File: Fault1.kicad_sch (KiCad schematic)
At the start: 45 parts

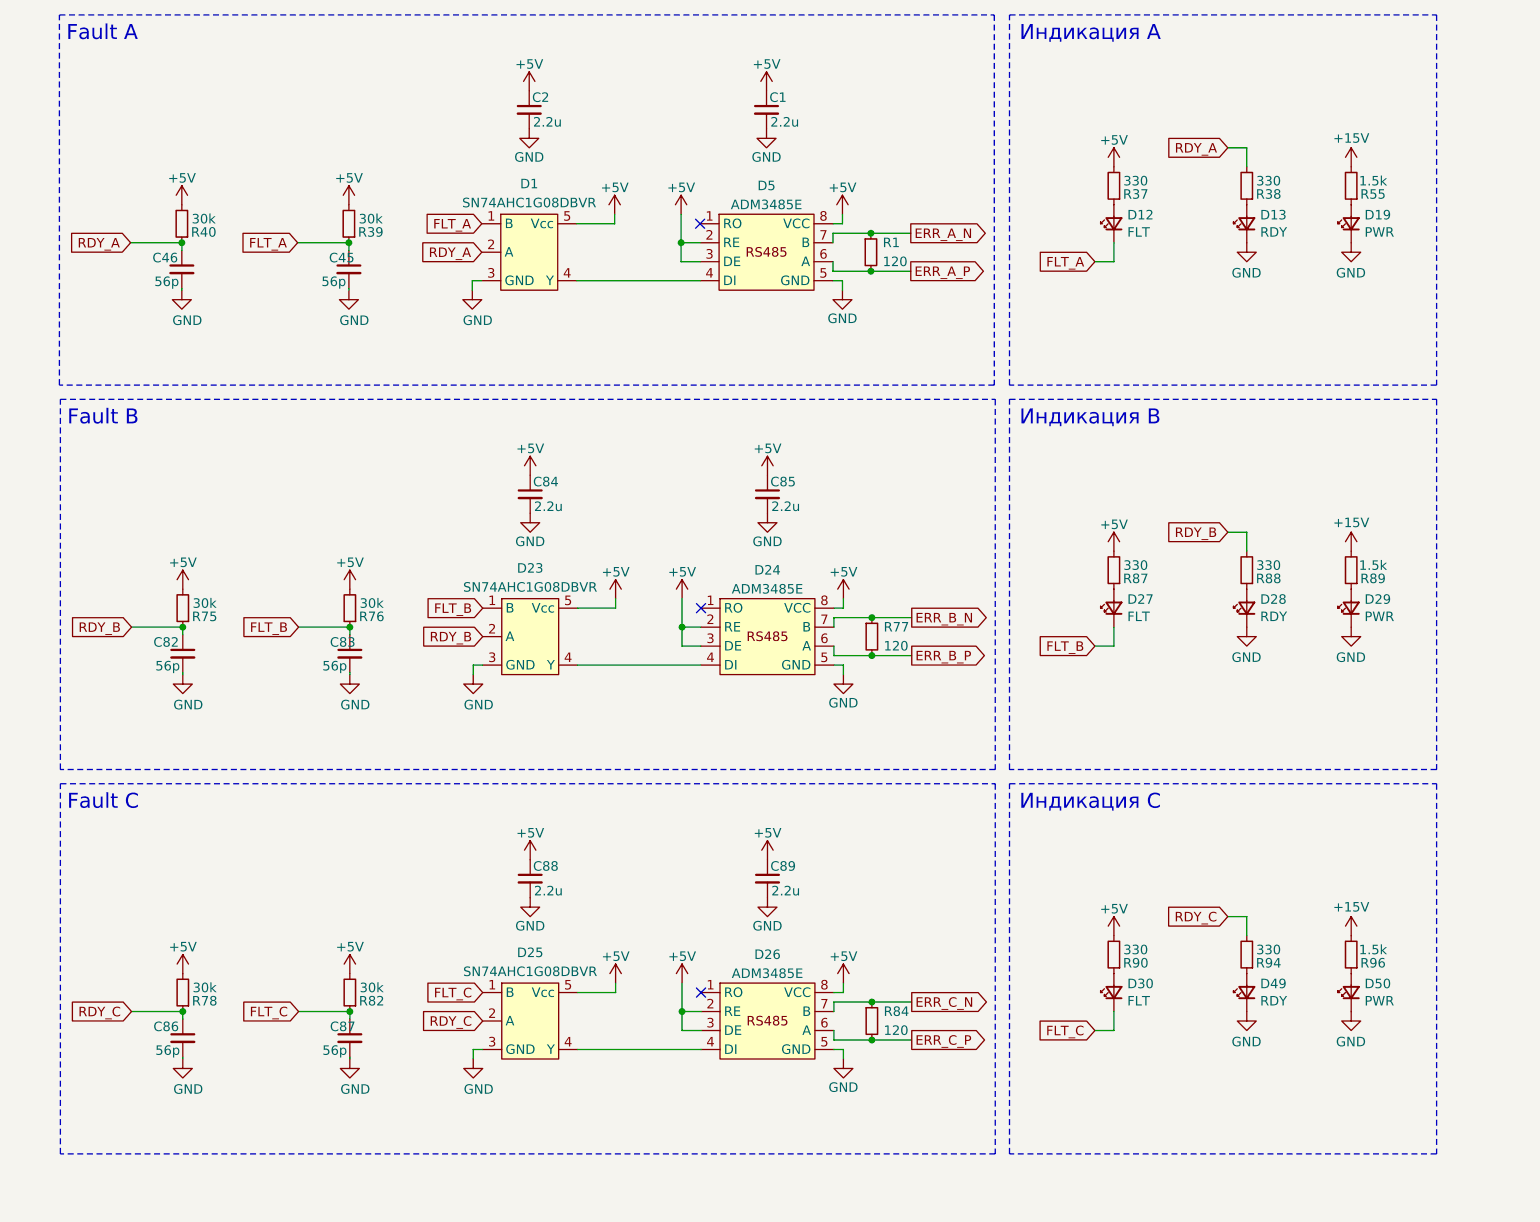
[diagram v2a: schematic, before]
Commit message: Исправления: исправил номиналы подтяжек и сопротивления светодиодов
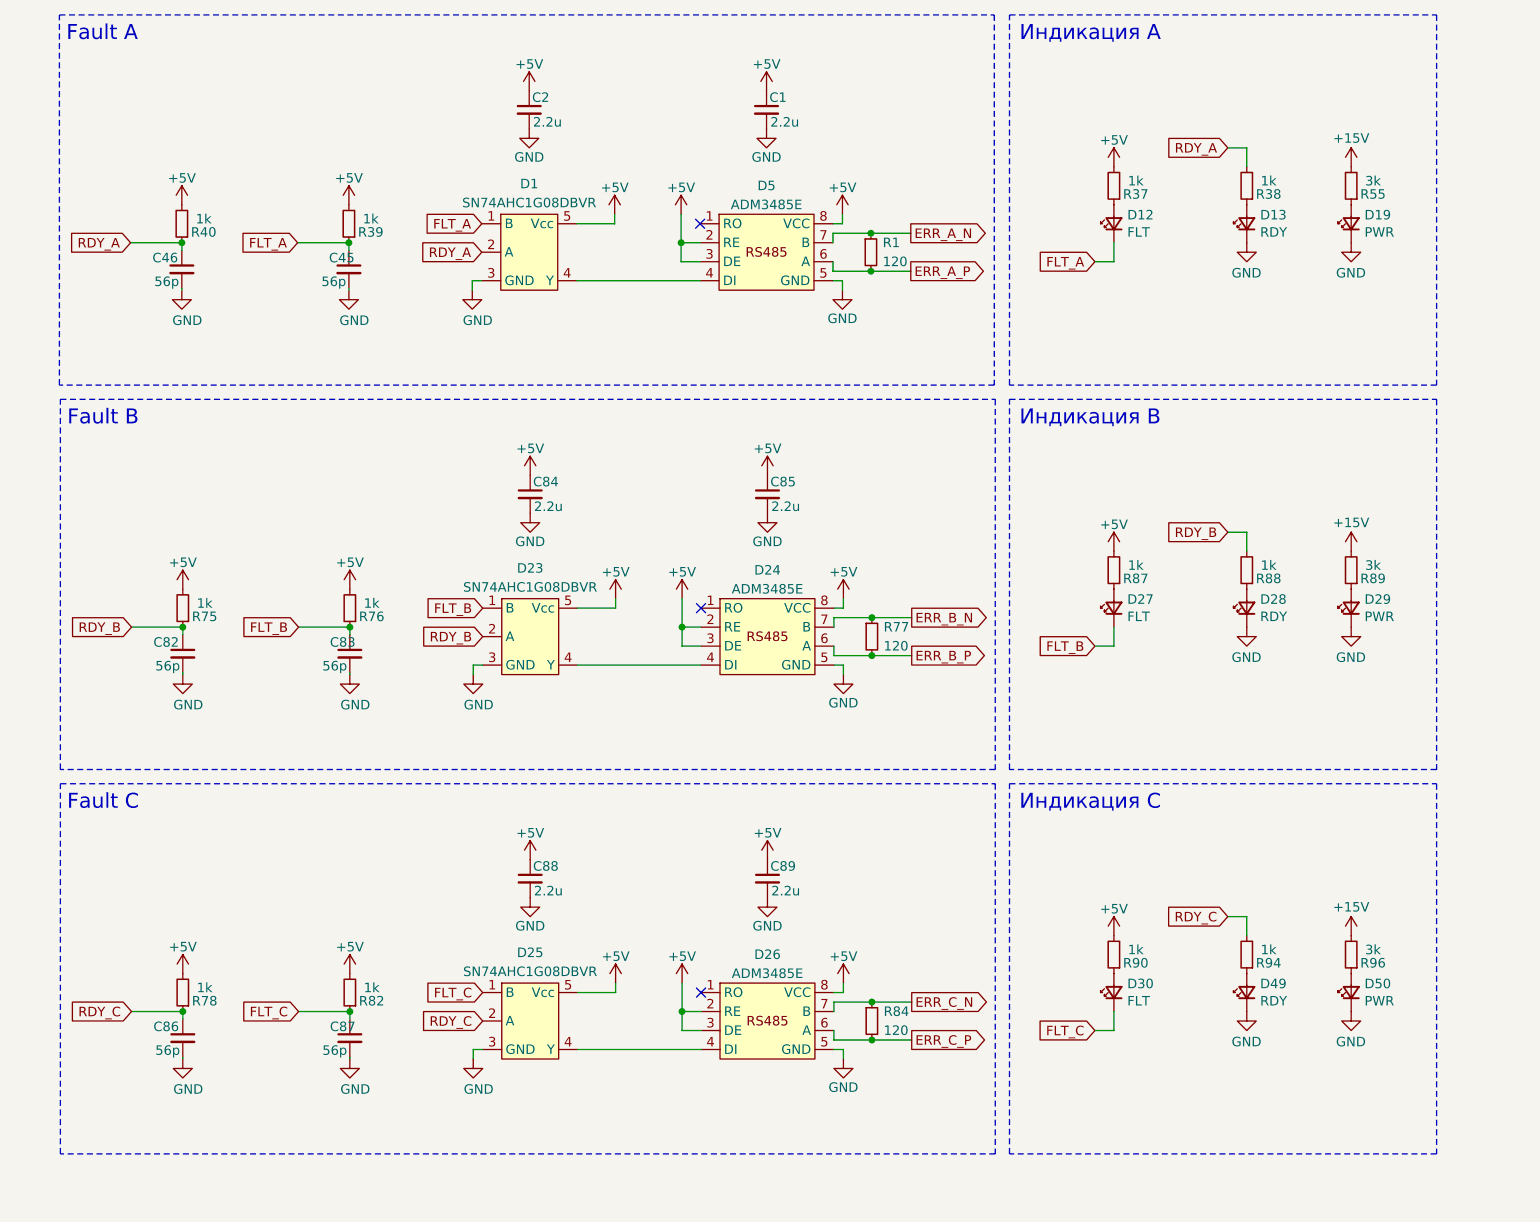
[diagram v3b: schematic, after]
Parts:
- R37, R38, R87, R88, R90, R94: value 330 -> 1k
- R39, R40, R75, R76, R78, R82: value 30k -> 1k
- R55, R89, R96: value 1.5k -> 3k
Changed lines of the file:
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@@
 			)
 		)
-		(property "Value" "30k"
+		(property "Value" "1k"
 			(at 35.687 44.45 0)
 			(effects
@@
 			)
 		)
-		(property "Value" "330"
+		(property "Value" "1k"
 			(at 160.401 142.24 0)
 			(effects
@@
 			)
 		)
-		(property "Value" "30k"
+		(property "Value" "1k"
 			(at 35.814 147.32 0)
 			(effects
@@
 			)
 		)
-		(property "Value" "30k"
+		(property "Value" "1k"
 			(at 58.166 95.885 0)
 			(effects
@@
 			)
 		)
-		(property "Value" "30k"
+		(property "Value" "1k"
 			(at 58.039 44.45 0)
 			(effects
@@
 			)
 		)
-		(property "Value" "330"
+		(property "Value" "1k"
 			(at 178.181 39.37 0)
 			(effects
@@
 			)
 		)
-		(property "Value" "330"
+		(property "Value" "1k"
 			(at 178.181 90.805 0)
 			(effects
@@
 			)
 		)
-		(property "Value" "1.5k"
+		(property "Value" "3k"
 			(at 192.151 142.24 0)
 			(effects
@@
 			)
 		)
-		(property "Value" "1.5k"
+		(property "Value" "3k"
 			(at 192.151 90.805 0)
 			(effects
@@
 			)
 		)
-		(property "Value" "330"
+		(property "Value" "1k"
 			(at 160.401 39.37 0)
 			(effects
@@
 			)
 		)
-		(property "Value" "30k"
+		(property "Value" "1k"
 			(at 35.814 95.885 0)
 			(effects
@@
 			)
 		)
-		(property "Value" "30k"
+		(property "Value" "1k"
 			(at 58.166 147.32 0)
 			(effects
@@
 			)
 		)
-		(property "Value" "330"
+		(property "Value" "1k"
 			(at 160.401 90.805 0)
 			(effects
@@
 			)
 		)
-		(property "Value" "1.5k"
+		(property "Value" "3k"
 			(at 192.151 39.37 0)
 			(effects
@@
 			)
 		)
-		(property "Value" "330"
+		(property "Value" "1k"
 			(at 178.181 142.24 0)
 			(effects

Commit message: VER2.2: все изменения в списке изменений
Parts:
- D1, D23, D25: value SN74AHC1G08DBVR -> ~; Description P/N (none) -> AND; Product Name (none) -> SN74AHC1G08DBVR
- D12, D27, D30: value FLT -> ~; Description P/N (none) -> Red LED; Product Name (none) -> FYLS-0805URC; Purpose (none) -> FLT
- D13, D28, D49: value RDY -> ~; Description P/N (none) -> Blue LED; Product Name (none) -> FYLS-0805UBC; Purpose (none) -> RDY
- D19, D29, D50: value PWR -> ~; Description P/N (none) -> Yellow LED; Product Name (none) -> FYLS-0805UYC; Purpose (none) -> PWR
- D24, D26, D5: value ADM3485E -> ~; Description P/N (none) -> RS485; Product Name (none) -> SN65HVD3082EDR

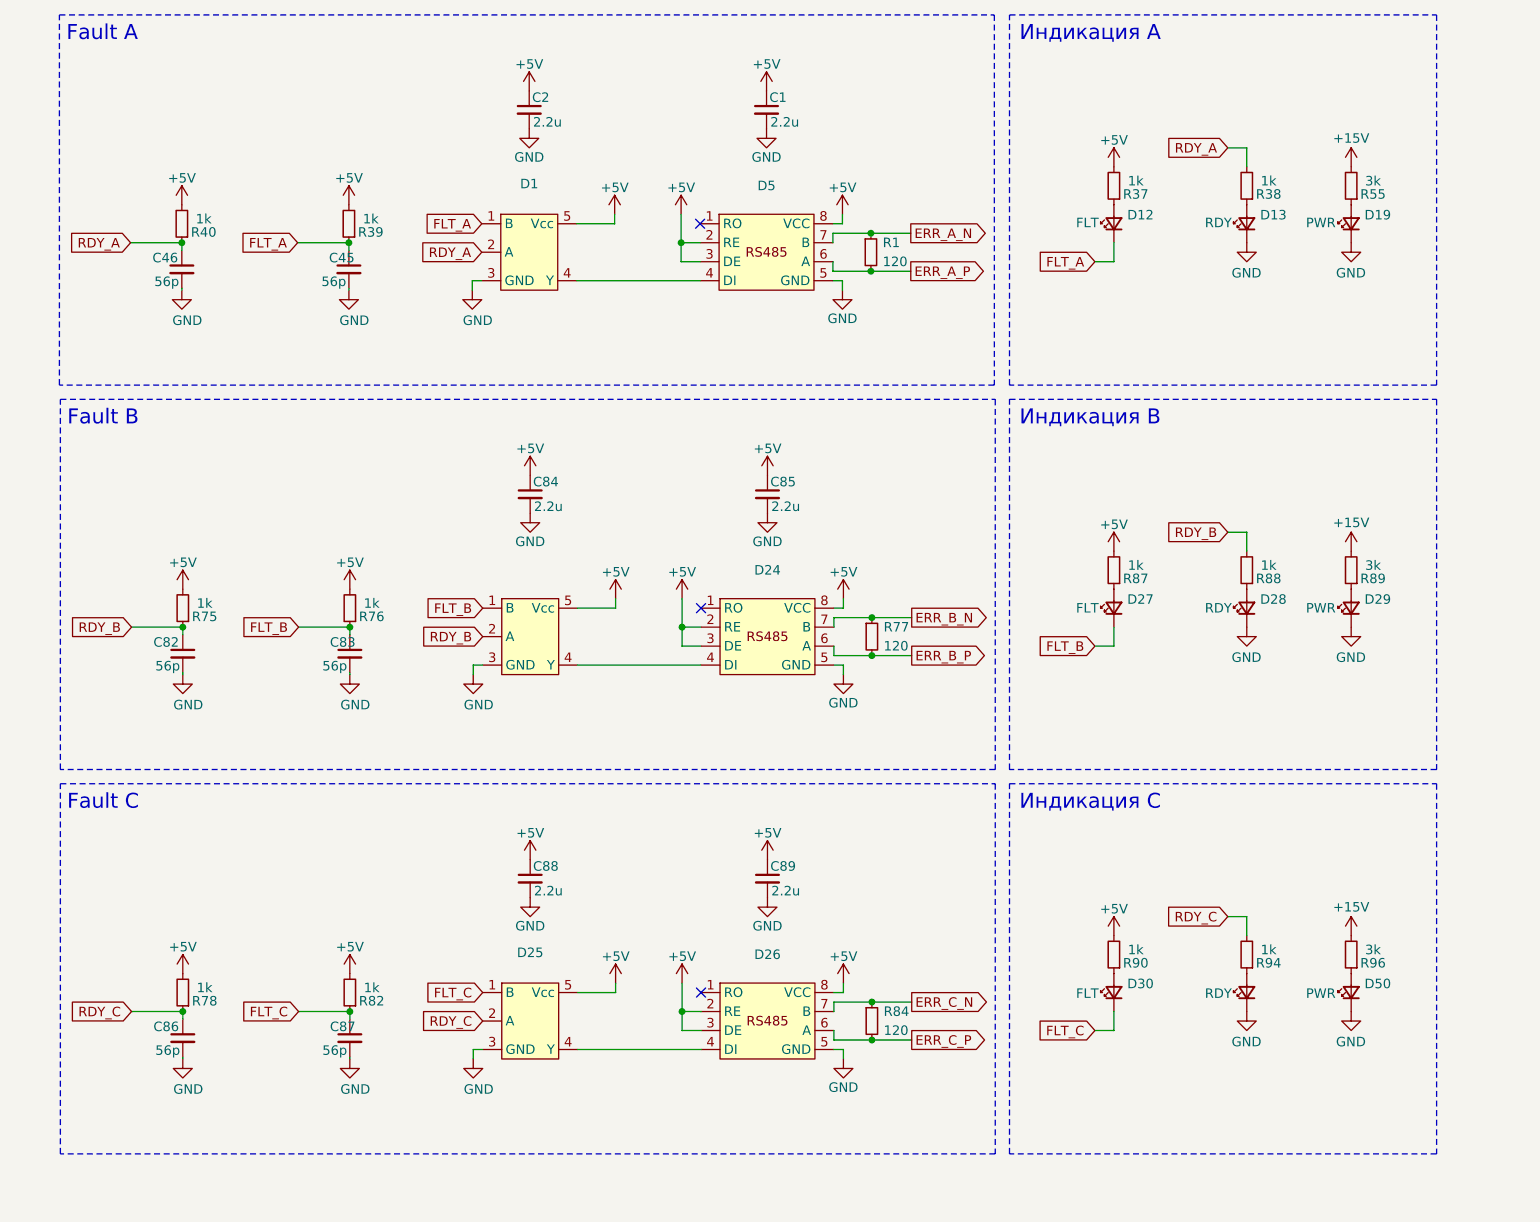
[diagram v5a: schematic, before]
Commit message: VER2.2: добавил фильтры на вход ШИМа и обновил все доки
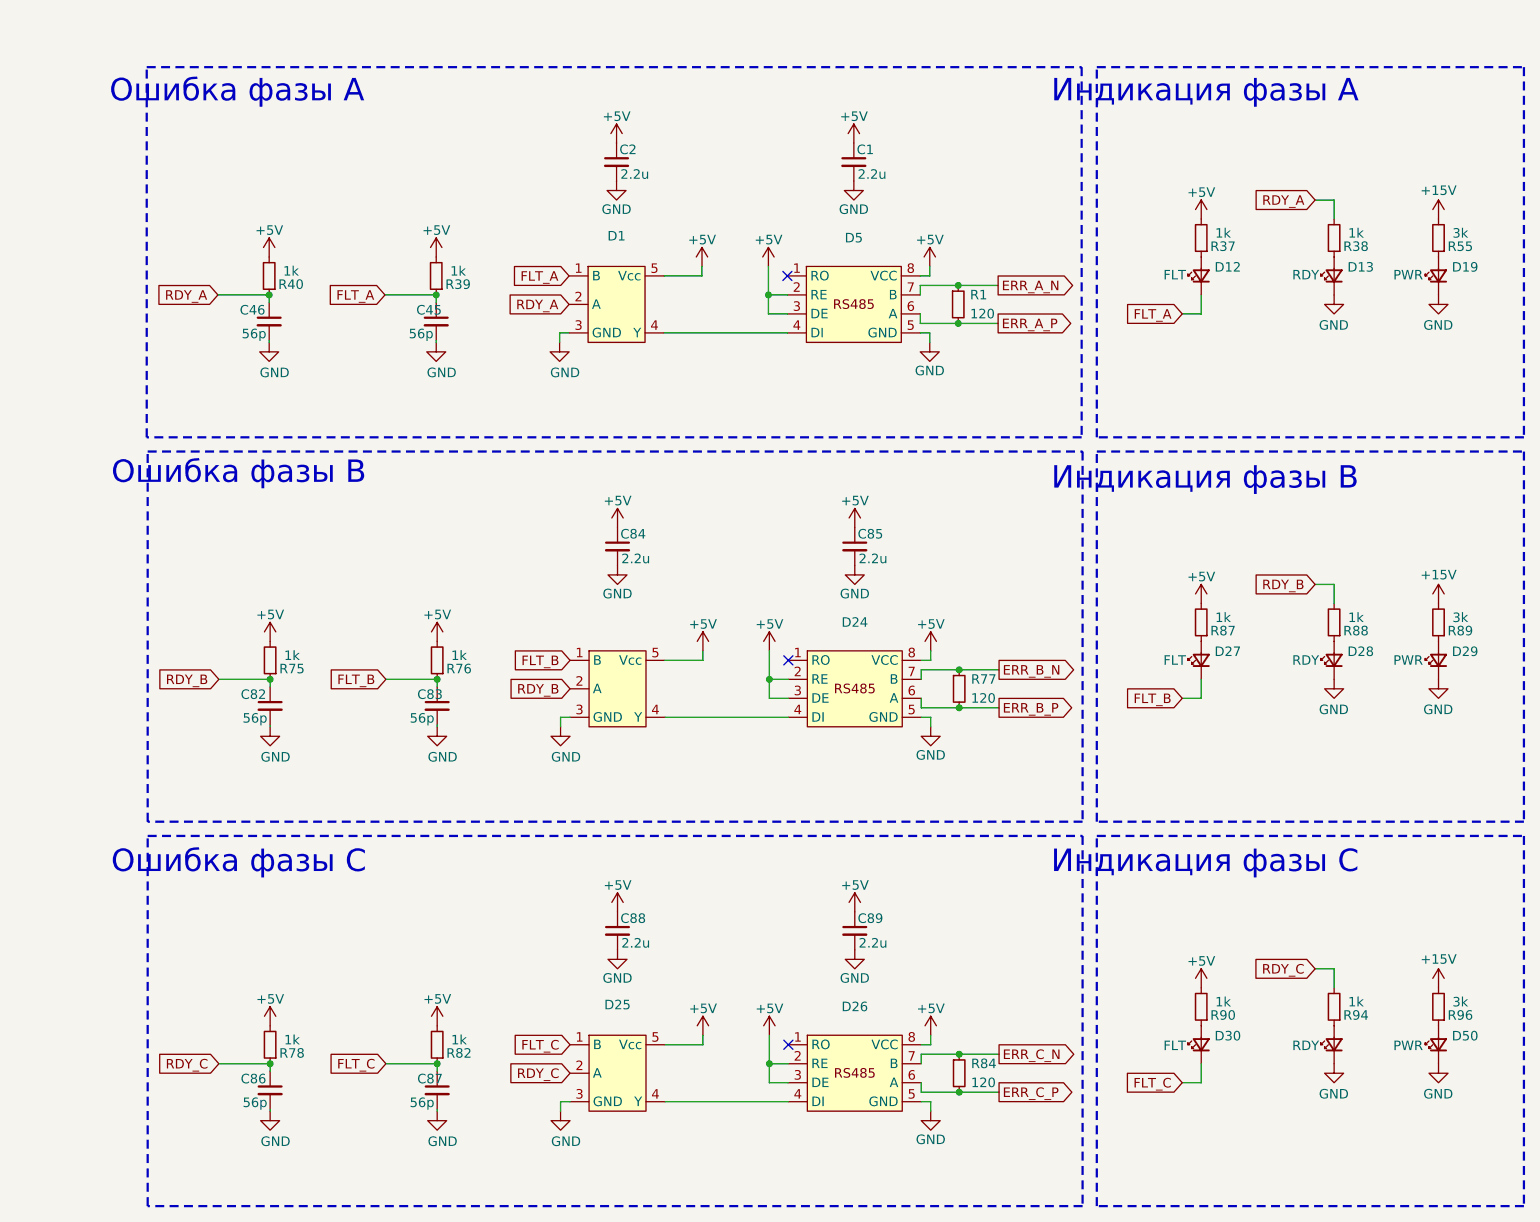
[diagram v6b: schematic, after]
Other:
- note added: "Индикация фазы A"
- note added: "Индикация фазы B"
- note added: "Индикация фазы C"
- note added: "Ошибка фазы А"
- note added: "Ошибка фазы В"
- note added: "Ошибка фазы С"
- note removed: "Fault A"
- note removed: "Fault B"
- note removed: "Fault C"
- note removed: "Индикация A"
- note removed: "Индикация B"
- note removed: "Индикация C"
- company: (none) -> ООО "ЭТТ"
- moved on the sheet: C1, C2, C45, C46, C82, C83, C84, C85, C86, C87, C88, C89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

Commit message: VER2.2.1: создал папку для производственных доков
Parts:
- C1, C2, C45, C46, C82, C83, C84, C85, C86, C87, C88, C89: Description P/N (none) -> Capacitor SMD 25+V
- R1, R37, R38, R39, R40, R55, R75, R76, R77, R78, R82, R84, R87, R88, R89, R90, R94, R96: Description P/N (none) -> Resistor SMD
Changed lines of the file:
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@@
 			)
 		)
-		(property "Description P/N" ""
+		(property "Description P/N" "Resistor SMD"
 			(at 44.45 52.07 0)
 			(effects
@@
 			)
 		)
-		(property "Description P/N" ""
+		(property "Description P/N" "Resistor SMD"
 			(at 169.164 149.86 0)
 			(effects
@@
 			)
 		)
-		(property "Description P/N" ""
+		(property "Description P/N" "Capacitor SMD 25+V"
 			(at 66.929 161.036 0)
 			(effects
@@
 			)
 		)
-		(property "Description P/N" ""
+		(property "Description P/N" "Resistor SMD"
 			(at 44.577 154.94 0)
 			(effects
@@
 			)
 		)
-		(property "Description P/N" ""
+		(property "Description P/N" "Resistor SMD"
 			(at 136.779 158.75 0)
 			(effects
@@
 			)
 		)
-		(property "Description P/N" ""
+		(property "Description P/N" "Resistor SMD"
 			(at 66.929 103.505 0)
 			(effects
@@
 			)
 		)
-		(property "Description P/N" ""
+		(property "Description P/N" "Resistor SMD"
 			(at 66.802 52.07 0)
 			(effects
@@
 			)
 		)
-		(property "Description P/N" ""
+		(property "Description P/N" "Resistor SMD"
 			(at 186.944 46.99 0)
 			(effects
@@
 			)
 		)
-		(property "Description P/N" ""
+		(property "Description P/N" "Capacitor SMD 25+V"
 			(at 91.059 139.7 0)
 			(effects
@@
 			)
 		)
-		(property "Description P/N" ""
+		(property "Description P/N" "Capacitor SMD 25+V"
 			(at 122.809 139.7 0)
 			(effects
@@
 			)
 		)
-		(property "Description P/N" ""
+		(property "Description P/N" "Resistor SMD"
 			(at 186.944 98.425 0)
 			(effects
@@
 			)
 		)
-		(property "Description P/N" ""
+		(property "Description P/N" "Resistor SMD"
 			(at 136.652 55.88 0)
 			(effects
@@
 			)
 		)
-		(property "Description P/N" ""
+		(property "Description P/N" "Capacitor SMD 25+V"
 			(at 66.929 109.601 0)
 			(effects
@@
 			)
 		)
-		(property "Description P/N" ""
+		(property "Description P/N" "Resistor SMD"
 			(at 200.914 149.86 0)
 			(effects
@@
 			)
 		)
-		(property "Description P/N" ""
+		(property "Description P/N" "Capacitor SMD 25+V"
 			(at 44.577 161.036 0)
 			(effects
@@
 			)
 		)
-		(property "Description P/N" ""
+		(property "Description P/N" "Resistor SMD"
 			(at 136.779 107.315 0)
 			(effects
@@
 			)
 		)
-		(property "Description P/N" ""
+		(property "Description P/N" "Resistor SMD"
 			(at 200.914 98.425 0)
 			(effects
@@
 			)
 		)
-		(property "Description P/N" ""
+		(property "Description P/N" "Resistor SMD"
 			(at 169.164 46.99 0)
 			(effects
@@
 			)
 		)
-		(property "Description P/N" ""
+		(property "Description P/N" "Capacitor SMD 25+V"
 			(at 91.059 88.265 0)
 			(effects
@@
 			)
 		)
-		(property "Description P/N" ""
+		(property "Description P/N" "Resistor SMD"
 			(at 44.577 103.505 0)
 			(effects
@@
 			)
 		)
-		(property "Description P/N" ""
+		(property "Description P/N" "Resistor SMD"
 			(at 66.929 154.94 0)
 			(effects
@@
 			)
 		)
-		(property "Description P/N" ""
+		(property "Description P/N" "Capacitor SMD 25+V"
 			(at 44.45 58.166 0)
 			(effects
@@
 			)
 		)
-		(property "Description P/N" ""
+		(property "Description P/N" "Resistor SMD"
 			(at 169.164 98.425 0)
 			(effects
@@
 			)
 		)
-		(property "Description P/N" ""
+		(property "Description P/N" "Capacitor SMD 25+V"
 			(at 122.809 88.265 0)
 			(effects
@@
 			)
 		)
-		(property "Description P/N" ""
+		(property "Description P/N" "Resistor SMD"
 			(at 200.914 46.99 0)
 			(effects
@@
 			)
 		)
-		(property "Description P/N" ""
+		(property "Description P/N" "Capacitor SMD 25+V"
 			(at 90.932 36.83 0)
 			(effects
@@
 			)
 		)
-		(property "Description P/N" ""
+		(property "Description P/N" "Capacitor SMD 25+V"
 			(at 122.682 36.83 0)
 			(effects
@@
 			)
 		)
-		(property "Description P/N" ""
+		(property "Description P/N" "Resistor SMD"
 			(at 186.944 149.86 0)
 			(effects
@@
 			)
 		)
-		(property "Description P/N" ""
+		(property "Description P/N" "Capacitor SMD 25+V"
 			(at 44.577 109.601 0)
 			(effects
@@
 			)
 		)
-		(property "Description P/N" ""
+		(property "Description P/N" "Capacitor SMD 25+V"
 			(at 66.802 58.166 0)
 			(effects
